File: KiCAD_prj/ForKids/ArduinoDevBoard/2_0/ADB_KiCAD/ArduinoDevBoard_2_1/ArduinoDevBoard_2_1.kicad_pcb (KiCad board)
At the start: 2 copper layers, 141.2 x 76.2 mm, 44 parts, among them J1 Conn_01x04_Female, J10 Conn_01x04_Female, J11 Conn_01x04_Female, J12 Conn_01x02_Female, J13 Conn_01x15_Female, J14 Conn_01x15_Female, J2 Conn_01x04_Female, J3 Conn_01x05_Female, J4 Screw_Terminal_01x02, J5 Conn_01x02_Female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

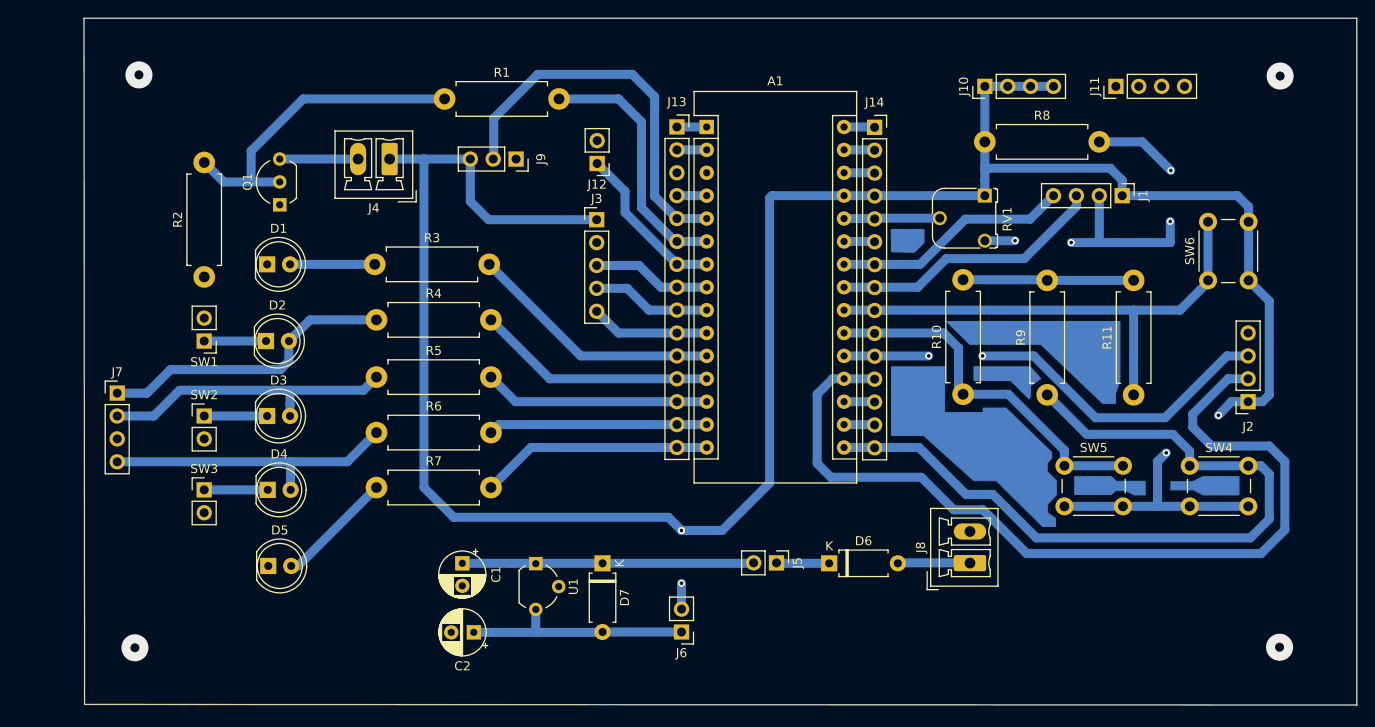
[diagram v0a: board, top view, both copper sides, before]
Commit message: Update Arduino Dev Board 2.1
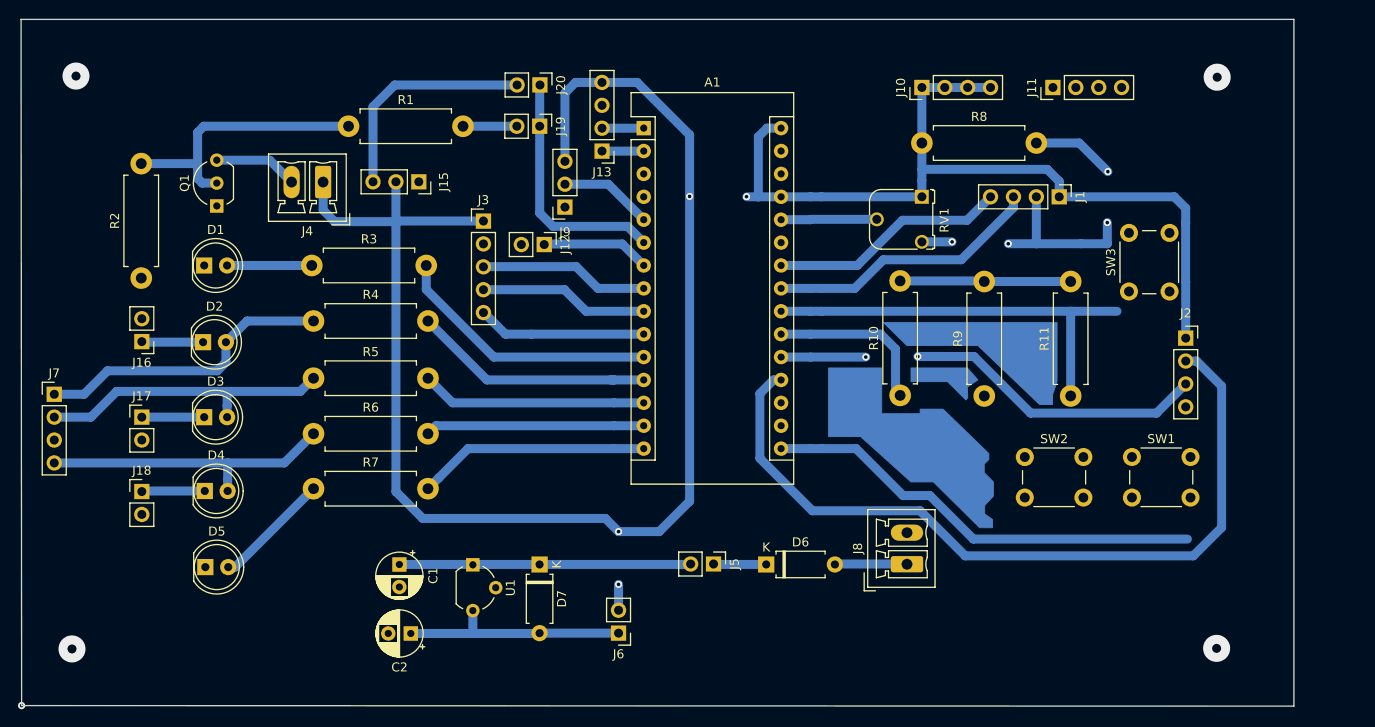
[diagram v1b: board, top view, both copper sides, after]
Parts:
- removed J14: Conn_01x15_Female, Connector_PinSocket_2.54mm:PinSocket_1x15_P2.54mm_Vertical
- removed SW4, SW5, SW6: SW_SPST, Button_Switch_THT:SW_PUSH_6mm_H5mm
- added J15: Conn_01x03_Female, Connector_PinSocket_2.54mm:PinSocket_1x03_P2.54mm_Vertical, F.Cu at (44.1, -58.1)
- added J16: Conn_01x02_Female, Connector_PinHeader_2.54mm:PinHeader_1x02_P2.54mm_Vertical, F.Cu at (13.3, -40.4)
- added J17: Conn_01x02_Female, Connector_PinHeader_2.54mm:PinHeader_1x02_P2.54mm_Vertical, F.Cu at (13.3, -32.0)
- added J18: Conn_01x02_Female, Connector_PinHeader_2.54mm:PinHeader_1x02_P2.54mm_Vertical, F.Cu at (13.3, -23.7)
- added J19: Conn_01x02_Female, Connector_PinHeader_2.54mm:PinHeader_1x02_P2.54mm_Vertical, F.Cu at (57.5, -64.3)
- added J20: Conn_01x02_Female, Connector_PinHeader_2.54mm:PinHeader_1x02_P2.54mm_Vertical, F.Cu at (57.5, -68.9)
- J13: value Conn_01x15_Female -> Conn_01x04_Female; footprint Connector_PinSocket_2.54mm:PinSocket_1x15_P2.54mm_Vertical -> Connector_PinHeader_2.54mm:PinHeader_1x04_P2.54mm_Vertical
- SW1, SW2, SW3: value SW_SPST -> Button_Switch_THT:SW_PUSH_6mm_H5mm; footprint Connector_PinHeader_2.54mm:PinHeader_1x02_P2.54mm_Vertical -> Button_Switch_THT:SW_PUSH_6mm
- moved SW3 104.9 mm to (122.9, -45.9), turned to 90 degrees
- moved SW1 103.7 mm to (123.2, -27.6), turned to 0 degrees
- moved SW2 91.2 mm to (111.3, -27.6)
- moved J3 12.6 mm to (51.2, -53.8)
- moved R1 11.1 mm to (36.3, -64.3)
- moved J12 10.7 mm to (58.0, -51.2), turned to 270 degrees
- moved J2 9.88 mm to (129.2, -40.8), turned to 0 degrees
- moved J13 8.73 mm to (64.4, -61.5), turned to 180 degrees
- moved J4 7.81 mm to (33.5, -58.1)
- moved J9 7.60 mm to (60.3, -55.3), turned to 180 degrees
- moved J10 6.99 mm to (99.9, -68.6)
- moved R8 6.99 mm to (99.9, -62.4)
- moved RV1 6.99 mm to (99.9, -56.5)
- moved C1 6.99 mm to (41.9, -15.7)
- moved A1 6.99 mm to (69.0, -64.1)
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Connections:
- A1 pad 17: 3V3 -> +3V3
- A1 pad 18: AREF -> Net-(A1-Pad18)
- A1 pad 28: RST -> Net-(A1-Pad28)
- A1 pad 30: VIN -> +5V
- D6 pad 1: +12V -> VIN
- J13 pad 1: TX -> RX
- J13 pad 2: RX -> TX
- J13 pad 3: Net-(J13-Pad3) -> Earth
- J13 pad 4: Earth -> +5V
- J5 pad 1: +12V -> VIN
- R1 pad 2: D3 -> Net-(J19-Pad2)
- SW1 pad 1: Net-(D2-Pad1) -> D13
- SW1 pad 2: Earth -> Net-(SW1-Pad2)
- SW2 pad 1: Net-(D3-Pad1) -> A2
- SW2 pad 2: Earth -> Net-(SW2-Pad2)
- SW3 pad 1: Net-(D4-Pad1) -> A3
- SW3 pad 2: Earth -> Net-(SW3-Pad2)
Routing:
- net D13: track 86.4 -> 49.2 mm
- net D2: track 43.3 -> 10.4 mm
- net Net-(J15-Pad3): track 0.00 -> 25.3 mm
- net A2: track 40.8 -> 18.7 mm
- net +5V: track 272.9 -> 254.7 mm
- net A0: track 100.4 -> 88.0 mm
- net A3: track 57.8 -> 46.7 mm
- net Earth: track 56.8 -> 50.2 mm
- net D4: track 18.2 -> 12.1 mm
- net Net-(J19-Pad2): track 0.00 -> 5.97 mm
- net +12V: track 5.84 -> 0.00 mm
- net Net-(Q1-Pad2): track 36.6 -> 30.8 mm
- net D5: track 13.2 -> 18.8 mm
- net D6: track 13.2 -> 18.8 mm
- net D7: track 13.2 -> 18.8 mm
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
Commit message: Update Arduino Dev Board 2.1 fix resistor 4.7K
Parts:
- moved R8 22.8 mm to (79.2, -52.8), turned to 270 degrees
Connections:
- R8 pad 2: Earth -> D2
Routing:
- net Earth: track 50.2 -> 41.0 mm, vias 4 -> 3

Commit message: Update ArduinoDevBoard 2.1 project
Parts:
- removed J19: Conn_01x02_Female, Connector_PinHeader_2.54mm:PinHeader_1x02_P2.54mm_Vertical
- removed Q1: PN2222A, Package_TO_SOT_THT:TO-92_Inline_Wide
- removed R1: 100, Resistor_THT:R_Axial_DIN0411_L9.9mm_D3.6mm_P12.70mm_Horizontal
- removed R2: 1K, Resistor_THT:R_Axial_DIN0411_L9.9mm_D3.6mm_P12.70mm_Horizontal
- added J14: M-PWM, Connector_PinHeader_2.54mm:PinHeader_1x02_P2.54mm_Vertical, F.Cu at (38.5, -66.3)
- J1: value Conn_01x04_Female -> LCD1602
- J10: value Conn_01x04_Female -> +5V
- J11: value Conn_01x04_Female -> GND
- J12: value Conn_01x02_Female -> Buzzer
- J13: value Conn_01x04_Female -> Bluetooth
- J15: value Conn_01x03_Female -> Servo SG90
- J2: value Conn_01x04_Female -> HC-SR04
- J20: value Conn_01x02_Female -> M
- J3: value Conn_01x05_Female -> MAX7219
- J4: value Screw_Terminal_01x02 -> MOTOR; footprint Connector_Phoenix_MC:PhoenixContact_MCV_1,5_2-G-3.5_1x02_P3.50mm_Vertical -> Connector_PinHeader_2.54mm:PinHeader_1x02_P2.54mm_Vertical
- J8: value Screw_Terminal_01x02 -> OUT POWER
- J9: value Conn_01x03_Female -> LM35
- R8: value 4.7K -> 10K
- SW1, SW2, SW3: value Button_Switch_THT:SW_PUSH_6mm_H5mm -> SW_Push_Dual
- moved J9 35.0 mm to (92.6, -68.8), turned to 0 degrees
- moved J7 32.2 mm to (25.3, -58.4), turned to 270 degrees
- moved J2 27.4 mm to (121.7, -14.4), turned to 270 degrees
- moved SW2 22.8 mm to (89.7, -34.9), turned to 90 degrees
- moved SW3 22.2 mm to (101.9, -38.7)
- moved J4 19.9 mm to (49.6, -69.8), turned to 90 degrees
- moved J1 18.4 mm to (98.3, -49.0)
- moved R10 17.4 mm to (112.5, -43.2), turned to 0 degrees
- moved SW1 16.8 mm to (106.4, -28.8), turned to 180 degrees
- moved R11 16.3 mm to (112.5, -50.2), turned to 0 degrees
- moved J20 12.8 mm to (45.0, -66.3), turned to 0 degrees
- moved R9 5.74 mm to (112.5, -34.2), turned to 0 degrees
- moved J15 4.27 mm to (45.0, -53.9), turned to 180 degrees
- moved RV1 2.91 mm to (98.4, -58.9)
- moved R8 2.46 mm to (77.1, -51.7)
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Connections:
- net +3V3 renamed Net-(A1-Pad17)
- J4 pad 1: +5V -> Net-(J14-Pad2)
- J4 pad 2: Net-(J4-Pad2) -> D2
- J9 pad 1: Earth -> +5V
- J9 pad 2: D2 -> A6
- J9 pad 3: +5V -> Earth
- R8 pad 1: +5V -> A6
- R8 pad 2: D2 -> Earth
- SW1 pad 2: Net-(SW1-Pad2) -> +5V
- SW2 pad 2: Net-(SW2-Pad2) -> +5V
- SW3 pad 2: Net-(SW3-Pad2) -> +5V
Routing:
- net A6: track 0.00 -> 37.6 mm
- net +5V: track 254.7 -> 289.7 mm, vias 4 -> 0
- net A0: track 88.0 -> 54.1 mm
- net Net-(D4-Pad2): track 33.2 -> 65.0 mm
- net Net-(Q1-Pad2): track 30.8 -> 0.00 mm
- net A2: track 18.7 -> 44.6 mm
- net Net-(J14-Pad2): track 0.00 -> 20.9 mm
- net Net-(J15-Pad3): track 25.3 -> 4.70 mm
- net A4: track 30.7 -> 10.8 mm
- net A5: track 26.4 -> 6.57 mm
- net D13: track 49.2 -> 30.7 mm
- net A1: track 43.1 -> 57.8 mm, vias 2 -> 0
- net Net-(D3-Pad2): track 33.4 -> 48.0 mm
- net D2: track 10.4 -> 19.9 mm, vias 0 -> 2
- net Net-(J4-Pad2): track 9.30 -> 0.00 mm
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- added copper zone on B.Cu, net Earth

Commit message: Update ArduinoDevBoard 2.1. Upgrade pcb
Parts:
- moved J1 51.0 mm to (55.0, -22.1), turned to 90 degrees
- moved J4 15.6 mm to (34.4, -66.2), turned to 0 degrees
- moved R8 13.3 mm to (77.1, -65.0)
- moved J10 11.2 mm to (109.6, -68.8), turned to 0 degrees
- moved J12 4.20 mm to (60.9, -54.2)
- moved J11 2.14 mm to (112.2, -68.8), turned to 0 degrees
- moved J14 1.68 mm to (40.2, -66.3)
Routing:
- net D2: track 19.9 -> 112.7 mm, vias 2 -> 0
- net D3: track 32.3 -> 106.6 mm, vias 2 -> 0
- net +5V: track 289.7 -> 333.4 mm, vias 0 -> 2
- net A5: track 6.57 -> 44.0 mm
- net A4: track 10.8 -> 47.4 mm
- net Earth: track 49.1 -> 70.2 mm, vias 4 -> 2
- net Net-(J14-Pad2): track 20.9 -> 6.80 mm
- net A6: track 37.6 -> 33.4 mm
- net D4: track 12.1 -> 10.1 mm
- net D11: track 24.3 -> 25.7 mm
- net D12: track 25.8 -> 27.1 mm
- net A1: track 57.8 -> 57.2 mm

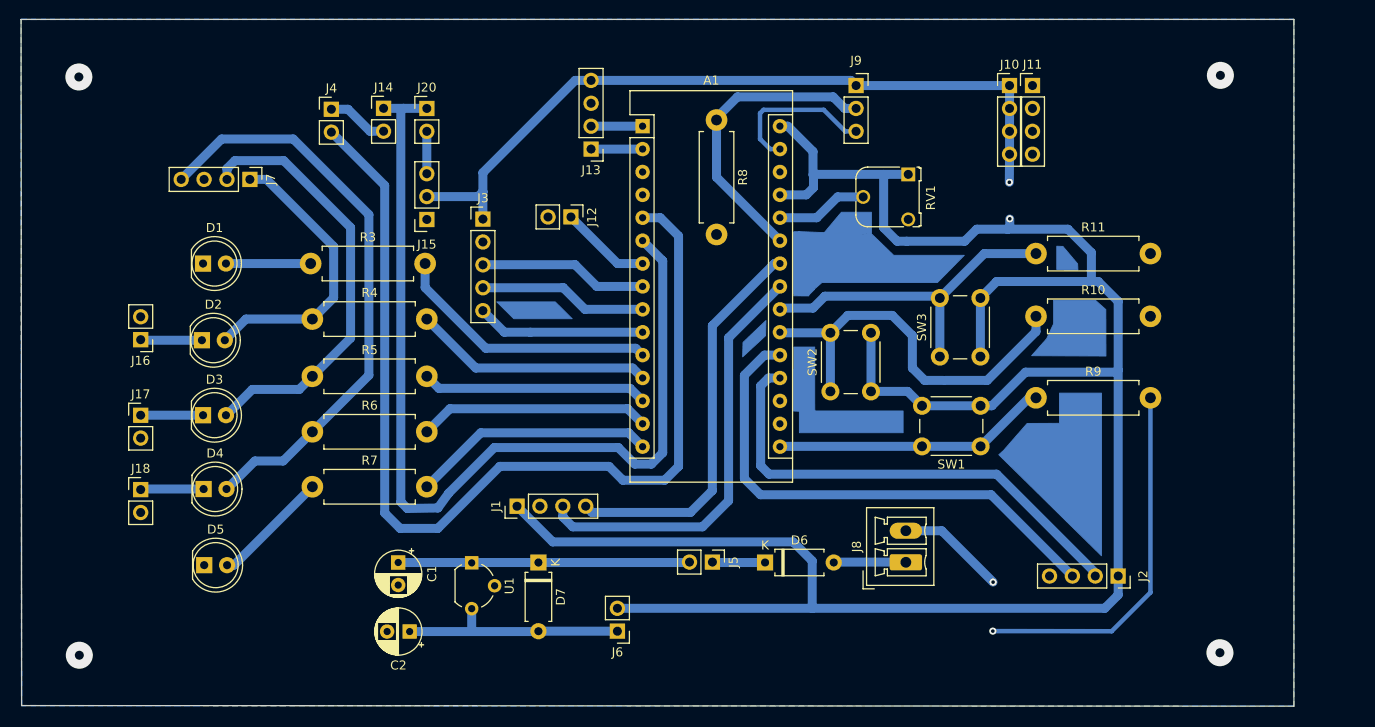
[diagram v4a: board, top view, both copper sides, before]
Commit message: Update ADB 2.1 end NanoMotors projects
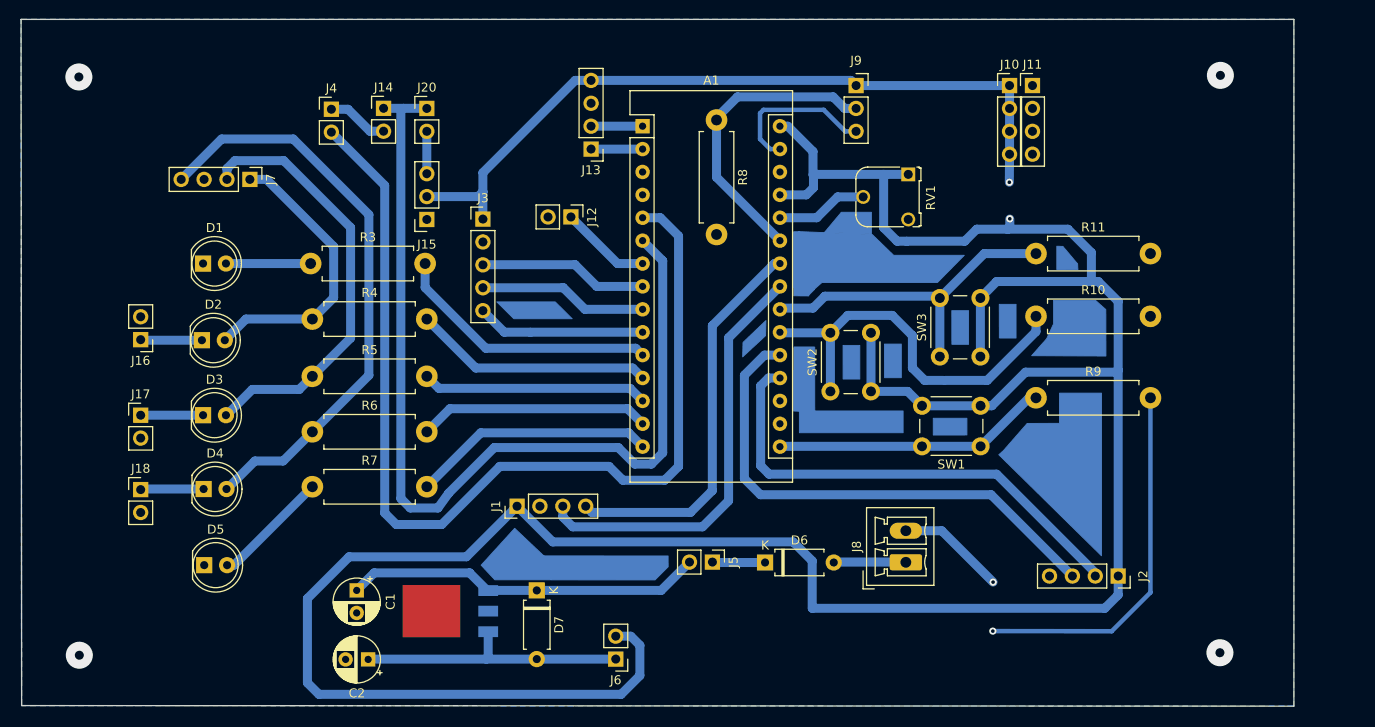
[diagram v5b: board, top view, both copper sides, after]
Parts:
- D1: value LED -> D8
- D2: value LED -> D9
- D3: value LED -> D10
- D4: value LED -> D11
- D5: value LED -> D12
- J16: value Conn_01x02_Female -> D9
- J17: value Conn_01x02_Female -> D10
- J18: value Conn_01x02_Female -> D11
- J20: value M -> Servo_Jamp
- J5: value Conn_01x02_Female -> VIN_JAMP_1
- J6: value Conn_01x02_Female -> VIN_JAMP_2
- J7: value Conn_01x04_Female -> RGB_LED
- J8: value OUT POWER -> VIN <= 12V
- SW1: value SW_Push_Dual -> D13
- SW2: value SW_Push_Dual -> D16
- SW3: value SW_Push_Dual -> D17
- U1: footprint Package_TO_SOT_THT:TO-92_Wide -> Package_TO_SOT_SMD:TO-252-3_TabPin2; moved to B.Cu
- moved U1 5.86 mm to (47.6, -10.5), turned to 180 degrees
- moved C2 5.55 mm to (38.4, -5.12)
- moved C1 5.55 mm to (37.2, -12.8)
- moved J6 3.10 mm to (65.9, -5.16)
- moved D7 3.10 mm to (57.2, -12.8)
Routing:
- net +5V: track 333.4 -> 393.4 mm
- net Net-(C1-Pad1): track 32.3 -> 39.9 mm
- net Net-(C2-Pad1): track 25.6 -> 30.6 mm
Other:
- board text added: "ARDUINO DEVELOPER BOARD v2.1"
- board text added: "POWER_OUT"

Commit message: Fix ArduinoDevBoard 2.0 project: add resistor 100 R to knob
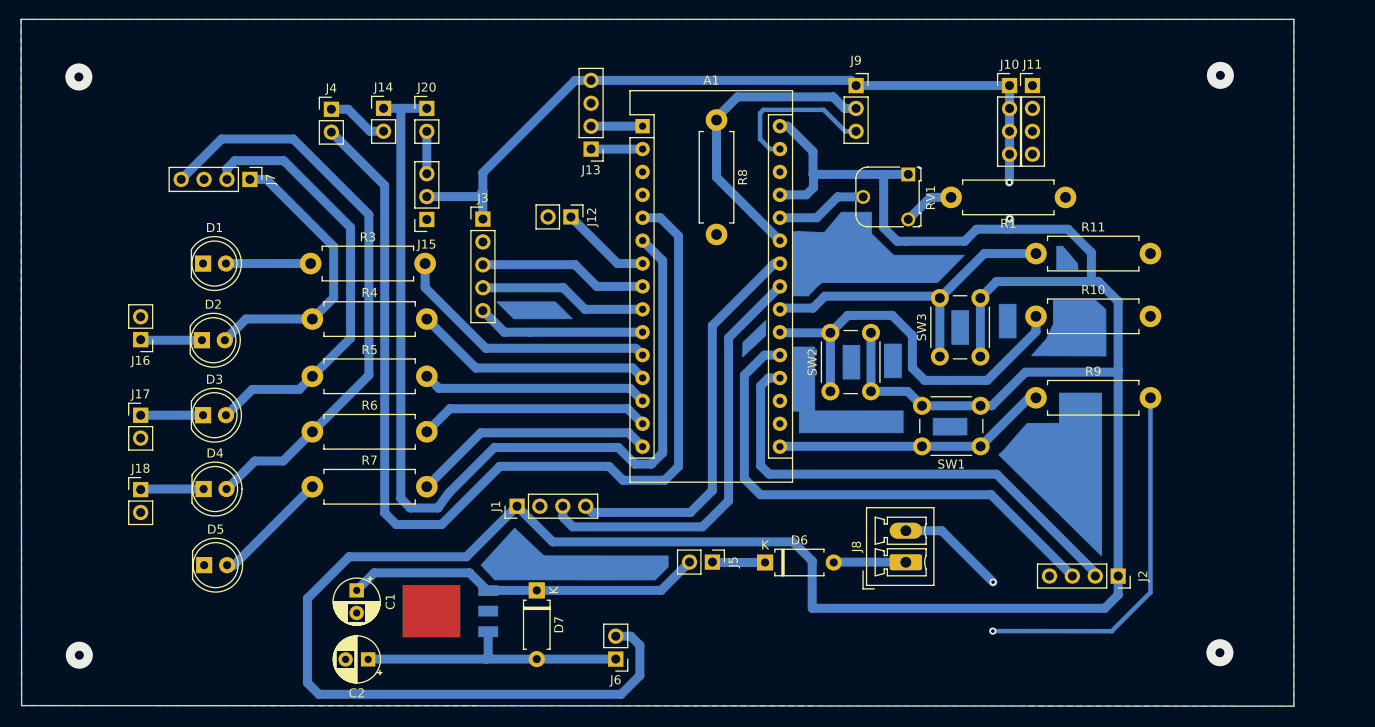
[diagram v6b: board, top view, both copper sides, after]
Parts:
- added R1: 100, Resistor_THT:R_Axial_DIN0411_L9.9mm_D3.6mm_P12.70mm_Horizontal, F.Cu at (115.8, -56.4)
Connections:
- RV1 pad 3: Earth -> Net-(R1-Pad2)
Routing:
- net Net-(R1-Pad2): track 0.00 -> 5.76 mm
